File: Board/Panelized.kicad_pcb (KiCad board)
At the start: 2 copper layers, 94.3 x 63.1 mm, 106 parts, among them CN1 Socket_BL600, CON1 USB-MINI-B, P1 CONN_01X17, P1 CONN_17, P2 CONN_4, P2 CONN_BL600_SWDIF, P3 CONN_01X17, P3 CONN_17, SW1 DIPSW_8, T1 CONN_1, T2 CONN_1, U1 93C56, U1 BL600, U2 FT232H, U3 TC7SZ125, U4 TC7SZ125, X1 12M

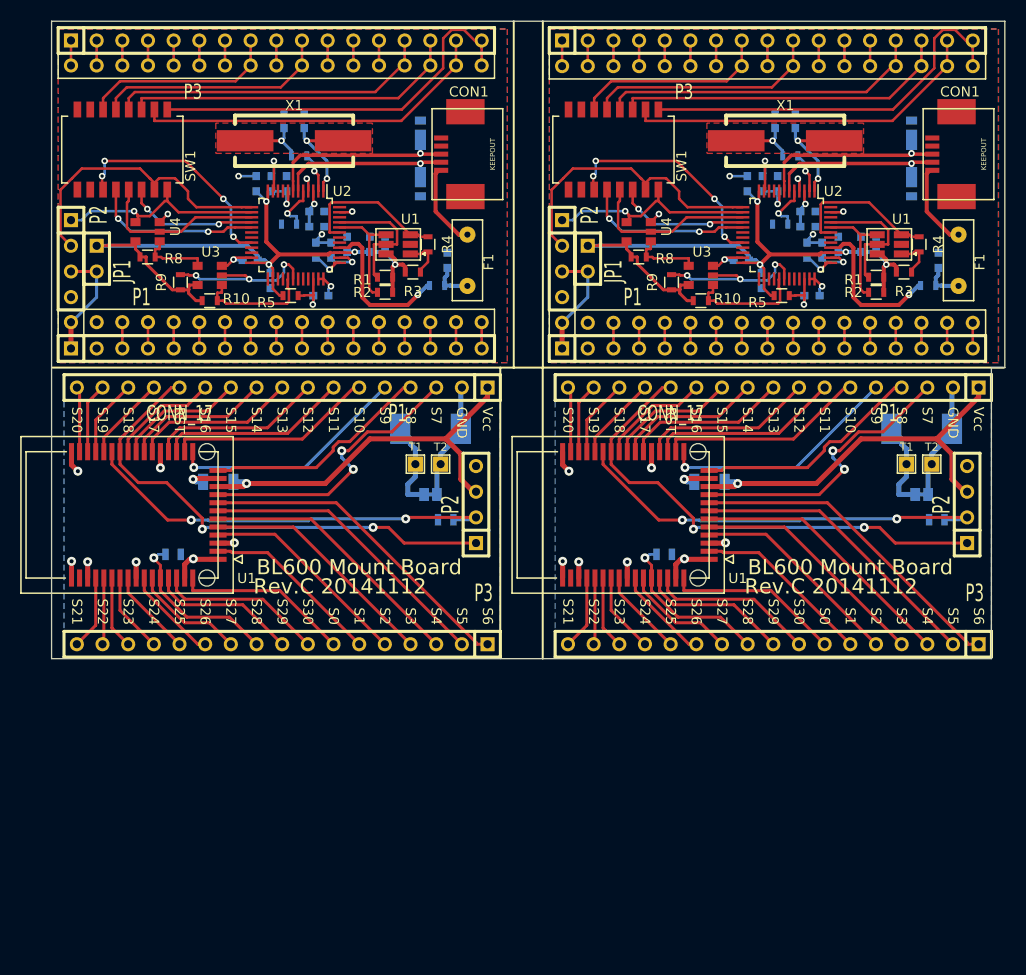
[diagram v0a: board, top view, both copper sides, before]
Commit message: U4のリファレンスを欠番になっていたU3に変更。 ACBUS4経由でBL600のリセットを行えるように信号追加。
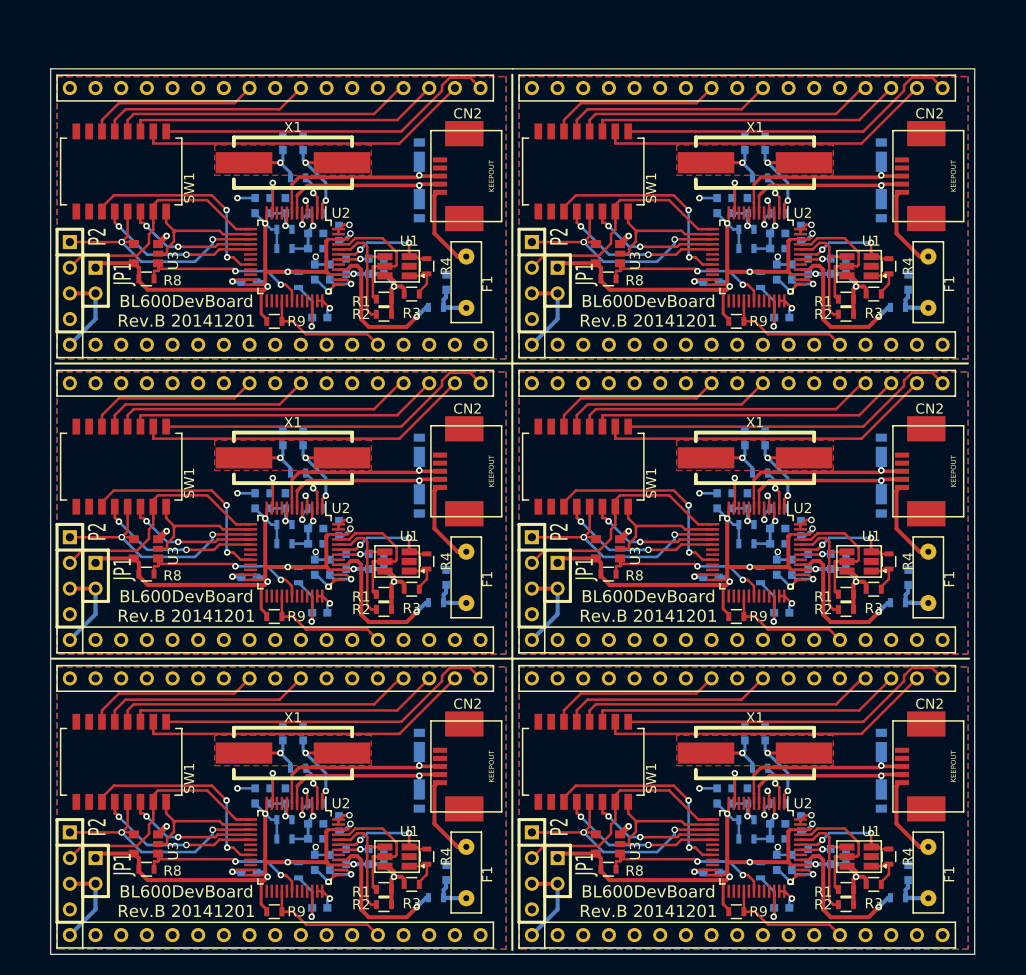
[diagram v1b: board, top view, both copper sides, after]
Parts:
- removed the C1 at (210.6, 41.5)
- removed the C1 at (194.1, 65.0)
- removed the C1 at (145.5, 65.0)
- removed the C1 at (162.0, 41.5)
- removed the C10 at (200.8, 35.5)
- removed the C10 at (152.2, 35.5)
- removed the C11 at (199.3, 35.5)
- removed the C11 at (150.8, 35.5)
- removed the C12 at (203.8, 38.2)
- removed the C12 at (155.2, 38.2)
- removed the C13 at (203.8, 39.8)
- removed the C13 at (155.2, 39.8)
- removed the C14 at (199.2, 45.1)
- removed the C14 at (150.7, 45.1)
- removed the C15 at (197.2, 43.1)
- removed the C15 at (148.7, 43.1)
- removed the C16 at (197.8, 35.5)
- removed the C16 at (149.2, 35.5)
- removed the C2 at (216.8, 43.1)
- removed the C2 at (168.2, 43.1)
- removed the C3 at (202.6, 29.2)
- removed the C3 at (154.0, 29.2)
- removed the C4 at (209.1, 41.5)
- removed the C4 at (160.5, 41.5)
- removed the C5 at (206.8, 41.5)
- removed the C5 at (158.2, 41.5)
- removed the C6 at (200.6, 29.2)
- removed the C6 at (152.0, 29.2)
- removed the C7 at (204.2, 46.6)
- removed the C7 at (155.7, 46.6)
- removed the C8 at (205.2, 42.1)
- removed the C8 at (156.7, 42.1)
- removed the C9 at (203.8, 42.1)
- removed the C9 at (155.2, 42.1)
- removed the CN1 at (222.7, 36.6)
- removed the CN1 at (174.1, 36.5)
- removed CON1 (x2): USB-MINI-B, AVR32Board:HIROSE_UX60SC-MB-5ST
- removed the D1 at (214.1, 30.5)
- removed the D1 at (165.5, 30.5)
- removed the D2 at (214.1, 35.5)
- removed the D2 at (165.5, 35.5)
- removed the F1 at (218.8, 43.1)
- removed the F1 at (170.2, 43.1)
- removed the FB1 at (215.8, 45.6)
- removed the FB1 at (167.2, 45.6)
- removed GS1 (x2): GS2, BL600:GS2_CLOSED
- removed the JP1 at (182.1, 42.9)
- removed the JP1 at (133.5, 42.9)
- removed P1 (x2), P3 (x2): CONN_01X17, BL600:SIL-17
- removed P1 (x2), P3 (x2): CONN_17, BL600:SIL-17
- removed the P2 at (179.5, 42.9)
- removed the P2 at (219.6, 67.2)
- removed the P2 at (171.0, 67.2)
- removed the P2 at (130.9, 42.9)
- removed the R1 at (210.6, 44.8)
- removed the R1 at (189.6, 72.2)
- removed the R1 at (141.0, 72.2)
- removed the R1 at (162.0, 44.8)
- removed R10 (x2): 10k, Resistors_SMD:R_0603
- removed the R2 at (210.6, 46.2)
- removed the R2 at (216.6, 68.8)
- removed the R2 at (168.0, 68.8)
- removed the R2 at (162.0, 46.2)
- removed the R3 at (213.3, 44.2)
- removed the R3 at (215.1, 59.8)
- removed the R3 at (166.5, 59.8)
- removed the R3 at (164.8, 44.2)
- removed the R4 at (214.8, 41.5)
- removed the R4 at (166.2, 41.5)
- removed the R5 at (201.2, 46.6)
- removed the R5 at (152.7, 46.6)
- removed the R6 at (202.1, 32.8)
- removed the R6 at (153.5, 32.8)
- removed the R7 at (201.1, 39.5)
- removed the R7 at (152.5, 39.5)
- removed the R8 at (187.1, 42.8)
- removed the R8 at (138.5, 42.8)
- removed the R9 at (190.3, 45.2)
- removed the R9 at (141.8, 45.2)
- removed the SW1 at (184.6, 32.1)
- removed the SW1 at (136.0, 32.1)
- removed T1 (x2), T2 (x2): CONN_1, Connect:SIL-1
- removed the U1 at (213.1, 41.5)
- removed the U1 at (194.1, 62.0)
- removed the U1 at (145.5, 62.0)
- removed the U1 at (164.5, 41.5)
- removed the U2 at (201.8, 40.6)
- removed the U2 at (153.2, 40.6)
- removed the U3 at (193.2, 44.6)
- removed the U3 at (144.7, 44.6)
- removed U4 (x2): TC7SZ125, Housings_JEITA:SC-74A
- removed the X1 at (201.6, 31.2)
- removed the X1 at (153.0, 31.2)
- added C1: 10n, Capacitors_SMD:C_0603, B.Cu at (161.9, 72.9)
- added C1: 10n, Capacitors_SMD:C_0603, B.Cu at (161.9, 43.7)
- added C1: 10n, Capacitors_SMD:C_0603, B.Cu at (207.6, 72.9)
- added C1: 10n, Capacitors_SMD:C_0603, B.Cu at (207.6, 43.7)
- added C1: 10n, Capacitors_SMD:C_0603, B.Cu at (161.9, 102.1)
- added C1: 10n, Capacitors_SMD:C_0603, B.Cu at (207.6, 102.1)
- added C10: 4.7u, Capacitors_SMD:C_0603, B.Cu at (152.1, 66.9)
- added C10: 4.7u, Capacitors_SMD:C_0603, B.Cu at (152.1, 37.7)
- added C10: 4.7u, Capacitors_SMD:C_0603, B.Cu at (197.9, 66.9)
- added C10: 4.7u, Capacitors_SMD:C_0603, B.Cu at (197.9, 37.7)
- added C10: 4.7u, Capacitors_SMD:C_0603, B.Cu at (152.1, 96.1)
- added C10: 4.7u, Capacitors_SMD:C_0603, B.Cu at (197.9, 96.1)
- added C11: 100n, Capacitors_SMD:C_0603, B.Cu at (150.6, 66.9)
- added C11: 100n, Capacitors_SMD:C_0603, B.Cu at (150.6, 37.7)
- added C11: 100n, Capacitors_SMD:C_0603, B.Cu at (196.4, 66.9)
- added C11: 100n, Capacitors_SMD:C_0603, B.Cu at (196.4, 37.7)
- added C11: 100n, Capacitors_SMD:C_0603, B.Cu at (150.6, 96.1)
- added C11: 100n, Capacitors_SMD:C_0603, B.Cu at (196.4, 96.1)
- added C12: 4.7u, Capacitors_SMD:C_0603, B.Cu at (155.1, 69.6)
- added C12: 4.7u, Capacitors_SMD:C_0603, B.Cu at (155.1, 40.4)
- added C12: 4.7u, Capacitors_SMD:C_0603, B.Cu at (200.9, 69.6)
- added C12: 4.7u, Capacitors_SMD:C_0603, B.Cu at (200.9, 40.4)
- added C12: 4.7u, Capacitors_SMD:C_0603, B.Cu at (155.1, 98.8)
- added C12: 4.7u, Capacitors_SMD:C_0603, B.Cu at (200.9, 98.8)
- added C13: 100n, Capacitors_SMD:C_0603, B.Cu at (155.1, 71.1)
- added C13: 100n, Capacitors_SMD:C_0603, B.Cu at (155.1, 41.9)
- added C13: 100n, Capacitors_SMD:C_0603, B.Cu at (200.9, 71.1)
- added C13: 100n, Capacitors_SMD:C_0603, B.Cu at (200.9, 41.9)
- added C13: 100n, Capacitors_SMD:C_0603, B.Cu at (155.1, 100.3)
- added C13: 100n, Capacitors_SMD:C_0603, B.Cu at (200.9, 100.3)
- added C14: 100n, Capacitors_SMD:C_0603, B.Cu at (157.4, 69.6)
- added C14: 100n, Capacitors_SMD:C_0603, B.Cu at (157.4, 40.4)
- added C14: 100n, Capacitors_SMD:C_0603, B.Cu at (203.2, 69.6)
- added C14: 100n, Capacitors_SMD:C_0603, B.Cu at (203.2, 40.4)
- added C14: 100n, Capacitors_SMD:C_0603, B.Cu at (157.4, 98.8)
- added C14: 100n, Capacitors_SMD:C_0603, B.Cu at (203.2, 98.8)
- added C15: 100n, Capacitors_SMD:C_0603, B.Cu at (148.5, 74.5)
- added C15: 100n, Capacitors_SMD:C_0603, B.Cu at (148.5, 45.2)
- added C15: 100n, Capacitors_SMD:C_0603, B.Cu at (194.3, 74.5)
- added C15: 100n, Capacitors_SMD:C_0603, B.Cu at (194.3, 45.2)
- added C15: 100n, Capacitors_SMD:C_0603, B.Cu at (148.5, 103.7)
- added C15: 100n, Capacitors_SMD:C_0603, B.Cu at (194.3, 103.7)
- added C16: 100n, Capacitors_SMD:C_0603, B.Cu at (149.1, 66.9)
- added C16: 100n, Capacitors_SMD:C_0603, B.Cu at (149.1, 37.7)
- added C16: 100n, Capacitors_SMD:C_0603, B.Cu at (194.9, 66.9)
- added C16: 100n, Capacitors_SMD:C_0603, B.Cu at (194.9, 37.7)
- added C16: 100n, Capacitors_SMD:C_0603, B.Cu at (149.1, 96.1)
- added C16: 100n, Capacitors_SMD:C_0603, B.Cu at (194.9, 96.1)
- added C2: 10n, Capacitors_SMD:C_0603, B.Cu at (168.0, 74.5)
- added C2: 10n, Capacitors_SMD:C_0603, B.Cu at (168.0, 45.2)
- added C2: 10n, Capacitors_SMD:C_0603, B.Cu at (213.8, 74.5)
- added C2: 10n, Capacitors_SMD:C_0603, B.Cu at (213.8, 45.2)
- added C2: 10n, Capacitors_SMD:C_0603, B.Cu at (168.0, 103.7)
- added C2: 10n, Capacitors_SMD:C_0603, B.Cu at (213.8, 103.7)
- added C3: 18p, Capacitors_SMD:C_0603, B.Cu at (153.9, 60.6)
- added C3: 18p, Capacitors_SMD:C_0603, B.Cu at (153.9, 31.4)
- added C3: 18p, Capacitors_SMD:C_0603, B.Cu at (199.6, 60.6)
- added C3: 18p, Capacitors_SMD:C_0603, B.Cu at (199.6, 31.4)
- added C3: 18p, Capacitors_SMD:C_0603, B.Cu at (153.9, 89.8)
- added C3: 18p, Capacitors_SMD:C_0603, B.Cu at (199.6, 89.8)
- added C4: 4.7u, Capacitors_SMD:C_0603, B.Cu at (160.4, 72.9)
- added C4: 4.7u, Capacitors_SMD:C_0603, B.Cu at (160.4, 43.7)
- added C4: 4.7u, Capacitors_SMD:C_0603, B.Cu at (206.1, 72.9)
- added C4: 4.7u, Capacitors_SMD:C_0603, B.Cu at (206.1, 43.7)
- added C4: 4.7u, Capacitors_SMD:C_0603, B.Cu at (160.4, 102.1)
- added C4: 4.7u, Capacitors_SMD:C_0603, B.Cu at (206.1, 102.1)
- added C5: 100n, Capacitors_SMD:C_0603, B.Cu at (158.1, 72.9)
- added C5: 100n, Capacitors_SMD:C_0603, B.Cu at (158.1, 43.7)
- added C5: 100n, Capacitors_SMD:C_0603, B.Cu at (203.9, 72.9)
- added C5: 100n, Capacitors_SMD:C_0603, B.Cu at (203.9, 43.7)
- added C5: 100n, Capacitors_SMD:C_0603, B.Cu at (158.1, 102.1)
- added C5: 100n, Capacitors_SMD:C_0603, B.Cu at (203.9, 102.1)
- added C6: 18p, Capacitors_SMD:C_0603, B.Cu at (151.9, 60.6)
- added C6: 18p, Capacitors_SMD:C_0603, B.Cu at (151.9, 31.4)
- added C6: 18p, Capacitors_SMD:C_0603, B.Cu at (197.6, 60.6)
- added C6: 18p, Capacitors_SMD:C_0603, B.Cu at (197.6, 31.4)
- added C6: 18p, Capacitors_SMD:C_0603, B.Cu at (151.9, 89.8)
- added C6: 18p, Capacitors_SMD:C_0603, B.Cu at (197.6, 89.8)
- added C7: 10n, Capacitors_SMD:C_0603, B.Cu at (155.5, 78.0)
- added C7: 10n, Capacitors_SMD:C_0603, B.Cu at (155.5, 48.7)
- added C7: 10n, Capacitors_SMD:C_0603, B.Cu at (201.3, 78.0)
- added C7: 10n, Capacitors_SMD:C_0603, B.Cu at (201.3, 48.7)
- added C7: 10n, Capacitors_SMD:C_0603, B.Cu at (155.5, 107.2)
- added C7: 10n, Capacitors_SMD:C_0603, B.Cu at (201.3, 107.2)
- added C8: 100n, Capacitors_SMD:C_0603, B.Cu at (156.5, 73.5)
- added C8: 100n, Capacitors_SMD:C_0603, B.Cu at (156.5, 44.2)
- added C8: 100n, Capacitors_SMD:C_0603, B.Cu at (202.3, 73.5)
- added C8: 100n, Capacitors_SMD:C_0603, B.Cu at (202.3, 44.2)
- added C8: 100n, Capacitors_SMD:C_0603, B.Cu at (156.5, 102.7)
- added C8: 100n, Capacitors_SMD:C_0603, B.Cu at (202.3, 102.7)
- added C9: 10n, Capacitors_SMD:C_0603, B.Cu at (155.0, 73.5)
- added C9: 10n, Capacitors_SMD:C_0603, B.Cu at (155.0, 44.2)
- added C9: 10n, Capacitors_SMD:C_0603, B.Cu at (200.8, 73.5)
- added C9: 10n, Capacitors_SMD:C_0603, B.Cu at (200.8, 44.2)
- added C9: 10n, Capacitors_SMD:C_0603, B.Cu at (155.0, 102.7)
- added C9: 10n, Capacitors_SMD:C_0603, B.Cu at (200.8, 102.7)
- added CN1: Socket_BL600, BL600:SOCKET_BL600, F.Cu at (174.0, 67.9)
- added CN1: Socket_BL600, BL600:SOCKET_BL600, F.Cu at (174.0, 38.7)
- added CN1: Socket_BL600, BL600:SOCKET_BL600, F.Cu at (219.7, 67.9)
- added CN1: Socket_BL600, BL600:SOCKET_BL600, F.Cu at (219.7, 38.7)
- added CN1: Socket_BL600, BL600:SOCKET_BL600, F.Cu at (174.0, 97.2)
- added CN1: Socket_BL600, BL600:SOCKET_BL600, F.Cu at (219.7, 97.2)
- added CN2: USB-MINI-B, AVR32Board:HIROSE_UX60SC-MB-5ST, F.Cu at (173.5, 64.0)
- added CN2: USB-MINI-B, AVR32Board:HIROSE_UX60SC-MB-5ST, F.Cu at (173.5, 34.7)
- added CN2: USB-MINI-B, AVR32Board:HIROSE_UX60SC-MB-5ST, F.Cu at (219.3, 64.0)
- added CN2: USB-MINI-B, AVR32Board:HIROSE_UX60SC-MB-5ST, F.Cu at (219.3, 34.7)
- added CN2: USB-MINI-B, AVR32Board:HIROSE_UX60SC-MB-5ST, F.Cu at (173.5, 93.2)
- added CN2: USB-MINI-B, AVR32Board:HIROSE_UX60SC-MB-5ST, F.Cu at (219.3, 93.2)
- added D1: UDZV15B, Diodes_SMD:Diode-TUMD2, B.Cu at (165.4, 61.9)
- added D1: UDZV15B, Diodes_SMD:Diode-TUMD2, B.Cu at (165.4, 32.7)
- added D1: UDZV15B, Diodes_SMD:Diode-TUMD2, B.Cu at (211.1, 61.9)
- added D1: UDZV15B, Diodes_SMD:Diode-TUMD2, B.Cu at (211.1, 32.7)
- added D1: UDZV15B, Diodes_SMD:Diode-TUMD2, B.Cu at (165.4, 91.1)
- added D1: UDZV15B, Diodes_SMD:Diode-TUMD2, B.Cu at (211.1, 91.1)
- added D2: UDZV15B, Diodes_SMD:Diode-TUMD2, B.Cu at (165.4, 66.9)
- added D2: UDZV15B, Diodes_SMD:Diode-TUMD2, B.Cu at (165.4, 37.7)
- added D2: UDZV15B, Diodes_SMD:Diode-TUMD2, B.Cu at (211.1, 66.9)
- added D2: UDZV15B, Diodes_SMD:Diode-TUMD2, B.Cu at (211.1, 37.7)
- added D2: UDZV15B, Diodes_SMD:Diode-TUMD2, B.Cu at (165.4, 96.1)
- added D2: UDZV15B, Diodes_SMD:Diode-TUMD2, B.Cu at (211.1, 96.1)
- added F1: RXEF050, TE_PolySW:RXEF050, F.Cu at (170.0, 74.5)
- added F1: RXEF050, TE_PolySW:RXEF050, F.Cu at (170.0, 45.2)
- added F1: RXEF050, TE_PolySW:RXEF050, F.Cu at (215.8, 74.5)
- added F1: RXEF050, TE_PolySW:RXEF050, F.Cu at (215.8, 45.2)
- added F1: RXEF050, TE_PolySW:RXEF050, F.Cu at (170.0, 103.7)
- added F1: RXEF050, TE_PolySW:RXEF050, F.Cu at (215.8, 103.7)
- added FB1: 470/1A, Resistors_SMD:R_0603, B.Cu at (167.0, 77.0)
- added FB1: 470/1A, Resistors_SMD:R_0603, B.Cu at (167.0, 47.7)
- added FB1: 470/1A, Resistors_SMD:R_0603, B.Cu at (212.8, 77.0)
- added FB1: 470/1A, Resistors_SMD:R_0603, B.Cu at (212.8, 47.7)
- added FB1: 470/1A, Resistors_SMD:R_0603, B.Cu at (167.0, 106.2)
- added FB1: 470/1A, Resistors_SMD:R_0603, B.Cu at (212.8, 106.2)
- added FB2: 470/1A, Resistors_SMD:R_0603, B.Cu at (152.0, 69.2)
- added FB2: 470/1A, Resistors_SMD:R_0603, B.Cu at (152.0, 40.0)
- added FB2: 470/1A, Resistors_SMD:R_0603, B.Cu at (197.8, 69.2)
- added FB2: 470/1A, Resistors_SMD:R_0603, B.Cu at (197.8, 40.0)
- added FB2: 470/1A, Resistors_SMD:R_0603, B.Cu at (152.0, 98.4)
- added FB2: 470/1A, Resistors_SMD:R_0603, B.Cu at (197.8, 98.4)
- added FB3: 470/1A, Resistors_SMD:R_0603, B.Cu at (152.0, 71.1)
- added FB3: 470/1A, Resistors_SMD:R_0603, B.Cu at (152.0, 41.9)
- added FB3: 470/1A, Resistors_SMD:R_0603, B.Cu at (197.8, 71.1)
- added FB3: 470/1A, Resistors_SMD:R_0603, B.Cu at (197.8, 41.9)
- added FB3: 470/1A, Resistors_SMD:R_0603, B.Cu at (152.0, 100.3)
- added FB3: 470/1A, Resistors_SMD:R_0603, B.Cu at (197.8, 100.3)
- added JP1: JUMPER, Connect:SIL-2, F.Cu at (133.3, 74.3)
- added JP1: JUMPER, Connect:SIL-2, F.Cu at (133.3, 45.1)
- added JP1: JUMPER, Connect:SIL-2, F.Cu at (179.1, 74.3)
- added JP1: JUMPER, Connect:SIL-2, F.Cu at (179.1, 45.1)
- added JP1: JUMPER, Connect:SIL-2, F.Cu at (133.3, 103.5)
- added JP1: JUMPER, Connect:SIL-2, F.Cu at (179.1, 103.5)
- added P2: CONN_BL600_SWDIF, Connect:SIL-4, F.Cu at (130.8, 74.3)
- added P2: CONN_BL600_SWDIF, Connect:SIL-4, F.Cu at (130.8, 45.1)
- added P2: CONN_BL600_SWDIF, Connect:SIL-4, F.Cu at (176.5, 74.3)
- added P2: CONN_BL600_SWDIF, Connect:SIL-4, F.Cu at (176.5, 45.1)
- added P2: CONN_BL600_SWDIF, Connect:SIL-4, F.Cu at (130.8, 103.5)
- added P2: CONN_BL600_SWDIF, Connect:SIL-4, F.Cu at (176.5, 103.5)
- added R1: 10k, Resistors_SMD:R_0603, F.Cu at (161.9, 76.1)
- added R1: 10k, Resistors_SMD:R_0603, F.Cu at (161.9, 46.9)
- added R1: 10k, Resistors_SMD:R_0603, F.Cu at (207.6, 76.1)
- added R1: 10k, Resistors_SMD:R_0603, F.Cu at (207.6, 46.9)
- added R1: 10k, Resistors_SMD:R_0603, F.Cu at (161.9, 105.3)
- added R1: 10k, Resistors_SMD:R_0603, F.Cu at (207.6, 105.3)
- added R2: 10k, Resistors_SMD:R_0603, F.Cu at (161.9, 77.6)
- added R2: 10k, Resistors_SMD:R_0603, F.Cu at (161.9, 48.4)
- added R2: 10k, Resistors_SMD:R_0603, F.Cu at (207.6, 77.6)
- added R2: 10k, Resistors_SMD:R_0603, F.Cu at (207.6, 48.4)
- added R2: 10k, Resistors_SMD:R_0603, F.Cu at (161.9, 106.8)
- added R2: 10k, Resistors_SMD:R_0603, F.Cu at (207.6, 106.8)
- added R3: 10k, Resistors_SMD:R_0603, F.Cu at (164.6, 75.6)
- added R3: 10k, Resistors_SMD:R_0603, F.Cu at (164.6, 46.4)
- added R3: 10k, Resistors_SMD:R_0603, F.Cu at (210.4, 75.6)
- added R3: 10k, Resistors_SMD:R_0603, F.Cu at (210.4, 46.4)
- added R3: 10k, Resistors_SMD:R_0603, F.Cu at (164.6, 104.8)
- added R3: 10k, Resistors_SMD:R_0603, F.Cu at (210.4, 104.8)
- added R4: 2k, Resistors_SMD:R_0603, F.Cu at (166.1, 72.9)
- added R4: 2k, Resistors_SMD:R_0603, F.Cu at (166.1, 43.7)
- added R4: 2k, Resistors_SMD:R_0603, F.Cu at (211.9, 72.9)
- added R4: 2k, Resistors_SMD:R_0603, F.Cu at (211.9, 43.7)
- added R4: 2k, Resistors_SMD:R_0603, F.Cu at (166.1, 102.1)
- added R4: 2k, Resistors_SMD:R_0603, F.Cu at (211.9, 102.1)
- added R5: 10k, Resistors_SMD:R_0603, B.Cu at (153.4, 74.2)
- added R5: 10k, Resistors_SMD:R_0603, B.Cu at (153.4, 45.0)
- added R5: 10k, Resistors_SMD:R_0603, B.Cu at (199.2, 74.2)
- added R5: 10k, Resistors_SMD:R_0603, B.Cu at (199.2, 45.0)
- added R5: 10k, Resistors_SMD:R_0603, B.Cu at (153.4, 103.4)
- added R5: 10k, Resistors_SMD:R_0603, B.Cu at (199.2, 103.4)
- added R6: 51, Resistors_SMD:R_0603, B.Cu at (153.4, 64.1)
- added R6: 51, Resistors_SMD:R_0603, B.Cu at (153.4, 34.9)
- added R6: 51, Resistors_SMD:R_0603, B.Cu at (199.1, 64.1)
- added R6: 51, Resistors_SMD:R_0603, B.Cu at (199.1, 34.9)
- added R6: 51, Resistors_SMD:R_0603, B.Cu at (153.4, 93.3)
- added R6: 51, Resistors_SMD:R_0603, B.Cu at (199.1, 93.3)
- added R7: 12k, Resistors_SMD:R_0603, B.Cu at (155.1, 67.6)
- added R7: 12k, Resistors_SMD:R_0603, B.Cu at (155.1, 38.4)
- added R7: 12k, Resistors_SMD:R_0603, B.Cu at (200.9, 67.6)
- added R7: 12k, Resistors_SMD:R_0603, B.Cu at (200.9, 38.4)
- added R7: 12k, Resistors_SMD:R_0603, B.Cu at (155.1, 96.8)
- added R7: 12k, Resistors_SMD:R_0603, B.Cu at (200.9, 96.8)
- added R8: 10k, Resistors_SMD:R_0603, F.Cu at (138.4, 74.1)
- added R8: 10k, Resistors_SMD:R_0603, F.Cu at (138.4, 44.9)
- added R8: 10k, Resistors_SMD:R_0603, F.Cu at (184.1, 74.1)
- added R8: 10k, Resistors_SMD:R_0603, F.Cu at (184.1, 44.9)
- added R8: 10k, Resistors_SMD:R_0603, F.Cu at (138.4, 103.3)
- added R8: 10k, Resistors_SMD:R_0603, F.Cu at (184.1, 103.3)
- added R9: 10k, Resistors_SMD:R_0603, F.Cu at (151.0, 78.3)
- added R9: 10k, Resistors_SMD:R_0603, F.Cu at (151.0, 49.1)
- added R9: 10k, Resistors_SMD:R_0603, F.Cu at (196.8, 78.3)
- added R9: 10k, Resistors_SMD:R_0603, F.Cu at (196.8, 49.1)
- added R9: 10k, Resistors_SMD:R_0603, F.Cu at (151.0, 107.5)
- added R9: 10k, Resistors_SMD:R_0603, F.Cu at (196.8, 107.5)
- added SW1: DIPSW_8, akiduki_switches:57D-0803, F.Cu at (135.9, 63.5)
- added SW1: DIPSW_8, akiduki_switches:57D-0803, F.Cu at (135.9, 34.3)
- added SW1: DIPSW_8, akiduki_switches:57D-0803, F.Cu at (181.6, 63.5)
- added SW1: DIPSW_8, akiduki_switches:57D-0803, F.Cu at (181.6, 34.3)
- added SW1: DIPSW_8, akiduki_switches:57D-0803, F.Cu at (135.9, 92.7)
- added SW1: DIPSW_8, akiduki_switches:57D-0803, F.Cu at (181.6, 92.7)
- added U1: 93C56, AVR32Board:SOT-23-6, F.Cu at (164.4, 72.9)
- added U1: 93C56, AVR32Board:SOT-23-6, F.Cu at (164.4, 43.7)
- added U1: 93C56, AVR32Board:SOT-23-6, F.Cu at (210.1, 72.9)
- added U1: 93C56, AVR32Board:SOT-23-6, F.Cu at (210.1, 43.7)
- added U1: 93C56, AVR32Board:SOT-23-6, F.Cu at (164.4, 102.1)
- added U1: 93C56, AVR32Board:SOT-23-6, F.Cu at (210.1, 102.1)
- added U2: FT232H, Housings_QFP:LQFP-48_7x7mm_Pitch0.5mm, F.Cu at (153.0, 72.0)
- added U2: FT232H, Housings_QFP:LQFP-48_7x7mm_Pitch0.5mm, F.Cu at (153.0, 42.7)
- added U2: FT232H, Housings_QFP:LQFP-48_7x7mm_Pitch0.5mm, F.Cu at (198.8, 72.0)
- added U2: FT232H, Housings_QFP:LQFP-48_7x7mm_Pitch0.5mm, F.Cu at (198.8, 42.7)
- added U2: FT232H, Housings_QFP:LQFP-48_7x7mm_Pitch0.5mm, F.Cu at (153.0, 101.2)
- added U2: FT232H, Housings_QFP:LQFP-48_7x7mm_Pitch0.5mm, F.Cu at (198.8, 101.2)
- added U3: TC7SZ125, Housings_JEITA:SC-74A, F.Cu at (138.3, 71.6)
- added U3: TC7SZ125, Housings_JEITA:SC-74A, F.Cu at (138.3, 42.4)
- added U3: TC7SZ125, Housings_JEITA:SC-74A, F.Cu at (184.1, 71.6)
- added U3: TC7SZ125, Housings_JEITA:SC-74A, F.Cu at (184.1, 42.4)
- added U3: TC7SZ125, Housings_JEITA:SC-74A, F.Cu at (138.3, 100.8)
- added U3: TC7SZ125, Housings_JEITA:SC-74A, F.Cu at (184.1, 100.8)
- added X1: 12M, Crystals:Crystal_HC49-SD_SMD, F.Cu at (152.9, 62.6)
- added X1: 12M, Crystals:Crystal_HC49-SD_SMD, F.Cu at (152.9, 33.4)
- added X1: 12M, Crystals:Crystal_HC49-SD_SMD, F.Cu at (198.6, 62.6)
- added X1: 12M, Crystals:Crystal_HC49-SD_SMD, F.Cu at (198.6, 33.4)
- added X1: 12M, Crystals:Crystal_HC49-SD_SMD, F.Cu at (152.9, 91.8)
- added X1: 12M, Crystals:Crystal_HC49-SD_SMD, F.Cu at (198.6, 91.8)
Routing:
- net /VCC3.3: track 139.8 -> 405.6 mm, vias 8 -> 36
- net Net-(CN1-Pad19): track 71.5 -> 199.9 mm
- net Net-(CN1-Pad18): track 78.8 -> 204.4 mm
- net Net-(CN1-Pad20): track 67.1 -> 186.1 mm
- net Net-(CN1-Pad21): track 64.9 -> 181.4 mm
- net Net-(CN2-Pad3): track 0.00 -> 115.4 mm, vias 0 -> 6
- net /TDO_RTS#: track 33.9 -> 146.8 mm, vias 0 -> 12
- net Net-(CN2-Pad2): track 0.00 -> 106.1 mm, vias 0 -> 6
- net /nRESET: track 99.5 -> 0.00 mm, vias 4 -> 0
- net /SWDCLK_TxD: track 57.8 -> 143.0 mm
- net /SWDCLK: track 84.1 -> 0.00 mm, vias 4 -> 0
- net /RI#: track 45.0 -> 127.6 mm, vias 8 -> 12
- net /TDI_RxD: track 0.00 -> 80.4 mm
- net /VCC: track 78.5 -> 0.00 mm, vias 2 -> 0
- net Net-(CN1-Pad25): track 46.8 -> 125.1 mm
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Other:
- board size 94.3 x 63.1 mm -> 91.4 x 87.6 mm
- board text added: "BL600DevBoard Rev.B 20141201"
- board text removed: "BL600 Mount Board"
- board text removed: "BL600DevBoard Rev.A 20141112"
- board text removed: "GND"
- board text removed: "RST"
- board text removed: "Rev.C 20141112"
- board text removed: "S0"
- board text removed: "S1"
- board text removed: "S10"
- board text removed: "S11"
- board text removed: "S12"
- board text removed: "S13"
- board text removed: "S14"
- board text removed: "S15"
- board text removed: "S16"
- board text removed: "S17"
- board text removed: "S18"
- board text removed: "S19"
- board text removed: "S2"
- board text removed: "S20"
- board text removed: "S21"
- board text removed: "S22"
- board text removed: "S23"
- board text removed: "S24"
- board text removed: "S25"
- board text removed: "S26"
- board text removed: "S27"
- board text removed: "S28"
- board text removed: "S29"
- board text removed: "S3"
- board text removed: "S30"
- board text removed: "S4"
- board text removed: "S5"
- board text removed: "S6"
- board text removed: "S7"
- board text removed: "S8"
- board text removed: "S9"
- board text removed: "Vcc"
